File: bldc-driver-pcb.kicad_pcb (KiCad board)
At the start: 4 copper layers, 50 x 50 mm, 92 parts, among them IC1 ATSAMD21G18A-AFT, IC2 AS5047P-ATSM, IC3 L6498D, IC4 L6498D, IC5 L6498D, IC6 AD8030ARZ, IC7 AD8030ARZ, J1 FTSH-105-XX-X-DV, J2 505567-0471, J3 505567-0671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

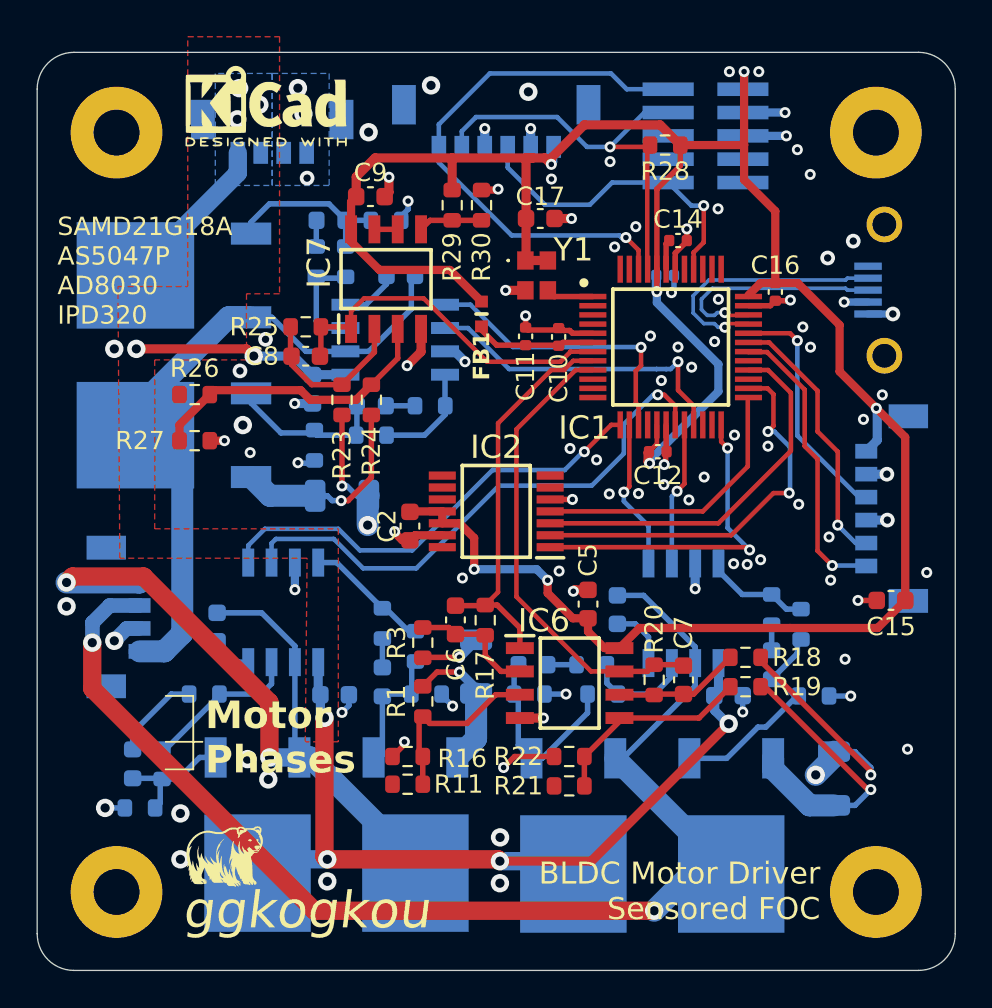
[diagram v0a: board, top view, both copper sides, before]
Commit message: Vmotor power plane
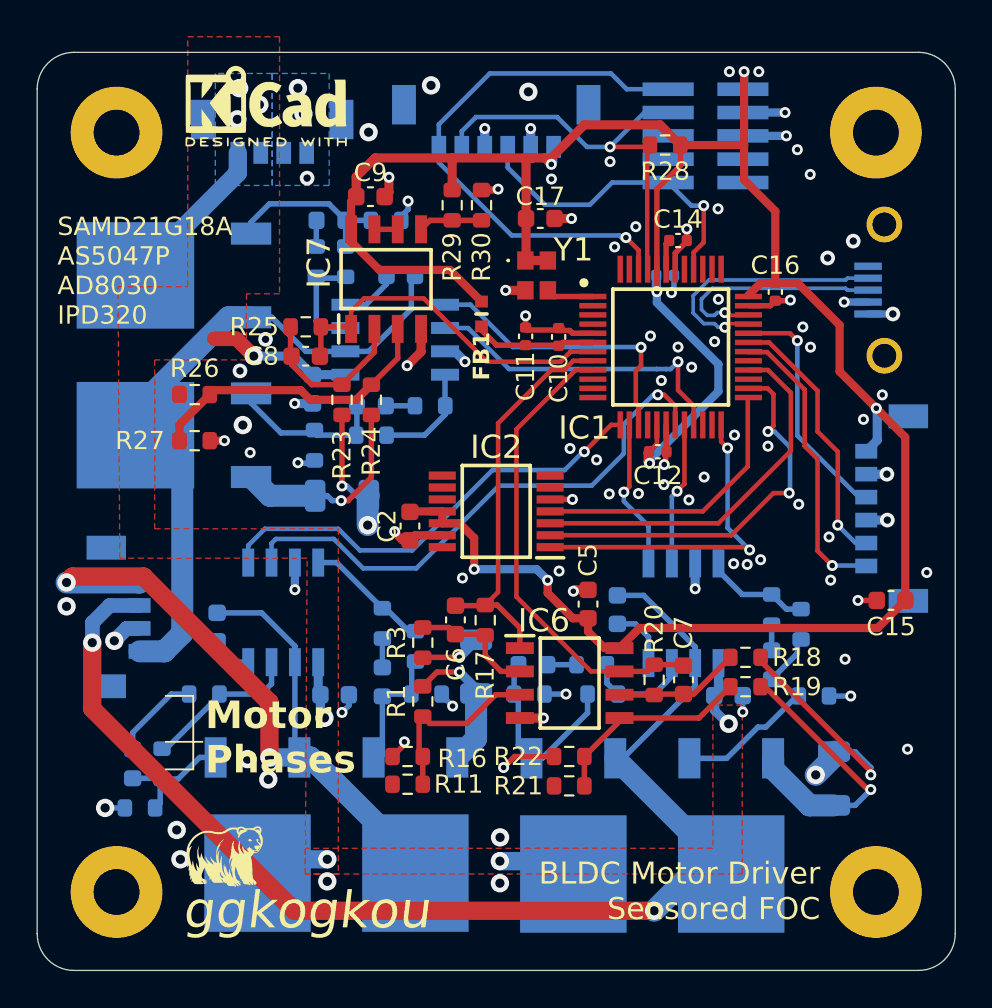
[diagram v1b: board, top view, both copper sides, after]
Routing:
- net VBUS: track 69.1 -> 32.3 mm, vias 9 -> 8
- net /Three-Phase Inverter/HALF_BRIDGE_2_OUT: track 69.6 -> 70.3 mm
- net GND: vias 104 -> 103
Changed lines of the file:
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@@
 		(tags "Connector")
 		(property "Reference" "J2"
-			(at 4 -3.2 0)
+			(at 5.8 1.8 0)
 			(layer "B.SilkS")
 			(effects
@@
 		(tags "resistor")
 		(property "Reference" "R14"
-			(at 1.05 1.2 270)
+			(at 0.05 1.25 270)
 			(layer "B.SilkS")
 			(effects
@@
 	)
 	(via
-		(at 122.8 116.9)
+		(at 122.6 117.8)
 		(size 1)
 		(drill 0.5)
@@
 	)
 	(via
-		(at 119.199997 91.6)
-		(size 1)
-		(drill 0.5)
-		(layers "F.Cu" "B.Cu")
-		(free yes)
-		(net 5)
-	)
-	(via
 		(at 149.9 91.499997)
 		(size 0.6)
@@
 	)
 	(segment
-		(start 145.177745 119.5)
-		(end 152.660638 112.017107)
-		(width 0.5)
-		(layer "F.Cu")
-		(net 11)
-	)
-	(segment
-		(start 130.644218 119.244218)
-		(end 130.8 119.4)
-		(width 1)
-		(layer "F.Cu")
-		(net 11)
-	)
-	(segment
-		(start 140.2 119.5)
-		(end 145.177745 119.5)
-		(width 0.5)
-		(layer "F.Cu")
-		(net 11)
-	)
-	(segment
 		(start 126.791806 91.99294)
-		(end 126.398866 91.6)
-		(width 0.5)
-		(layer "F.Cu")
-		(net 11)
-	)
-	(segment
-		(start 130.8 119.4)
-		(end 140.1 119.4)
-		(width 1)
-		(layer "F.Cu")
-		(net 11)
-	)
-	(segment
-		(start 126.398866 91.6)
-		(end 120.4 91.6)
-		(width 0.5)
-		(layer "F.Cu")
-		(net 11)
-	)
-	(segment
-		(start 140.1 119.4)
-		(end 140.2 119.5)
-		(width 1)
+		(end 125.848866 91.05)
+		(width 0.8)
 		(layer "F.Cu")
 		(net 11)
 	)
 	(segment
-		(start 130.644218 111.694087)
-		(end 130.644218 119.244218)
-		(width 1)
+		(start 125.848866 91.05)
+		(end 124.65 91.05)
+		(width 0.8)
 		(layer "F.Cu")
 		(net 11)
@@
 	)
 	(via
-		(at 120.4 91.6)
-		(size 1)
-		(drill 0.5)
-		(layers "F.Cu" "B.Cu")
-		(net 11)
-	)
-	(via
 		(at 140.2 119.5)
 		(size 1)
@@
 	)
 	(segment
-		(start 118 110.1)
-		(end 130.1 122.2)
+		(start 118 107.6)
+		(end 118 111.2)
 		(width 1)
 		(layer "F.Cu")
@@
 	)
 	(segment
-		(start 118 107.6)
-		(end 118 110.1)
+		(start 118 111.2)
+		(end 129 122.2)
 		(width 1)
 		(layer "F.Cu")
@@
 	)
 	(segment
-		(start 130.1 122.2)
+		(start 129 122.2)
 		(end 148.6 122.2)
 		(width 1)
@@
 			(pts
 				(xy 123.2 74.6) (xy 128.2 74.6) (xy 128.2 88.6) (xy 126.4 88.6) (xy 126.4 92.2) (xy 121.4 92.2)
-				(xy 121.4 101.4) (xy 131.4 101.4) (xy 131.4 113) (xy 129.6 113) (xy 129.7 103) (xy 119.5 103) (xy 119.4 88.2)
-				(xy 123.2 88.2)
+				(xy 121.4 101.4) (xy 131.4 101.4) (xy 131.4 120.2) (xy 129.6 120.2) (xy 129.7 103) (xy 119.5 103)
+				(xy 119.4 88.2) (xy 123.2 88.2)
+			)
+		)
+	)
+	(zone
+		(net 11)
+		(net_name "VBUS")
+		(layer "F.Cu")
+		(hatch edge 0.5)
+		(priority 5)
+		(connect_pads
+			(clearance 0.5)
+		)
+		(min_thickness 0.25)
+		(filled_areas_thickness no)
+		(fill yes
+			(thermal_gap 0.5)
+			(thermal_bridge_width 0.5)
+		)
+		(polygon
+			(pts
+				(xy 129.6 120.2) (xy 153.4 120.2) (xy 153.4 111) (xy 151.8 111) (xy 151.8 118.8) (xy 129.6 118.8)
 			)
 		)

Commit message: Layout QOL changes
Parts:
- moved R33 0.95 mm to (142.8, 110.4)
- moved C15 0.72 mm to (160.9, 105.8), turned to 0 degrees
- moved D3 0.70 mm to (142.7, 108.8)
- moved R7 0.62 mm to (145.8, 108.8)
- moved R1 0.43 mm to (136.0, 111.2)
- moved R11 0.41 mm to (135.2, 115.7)
- moved R31 0.37 mm to (121.0, 116.6)
- moved R16 0.34 mm to (135.2, 114.1)
- moved C5 0.23 mm to (145.1, 105.7), turned to 180 degrees
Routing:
- net /Three-Phase Inverter/HALF_BRIDGE_1_OUT: track 43.0 -> 37.5 mm
- net +3V3: track 141.2 -> 136.8 mm
- net GND: track 82.0 -> 83.7 mm, vias 103 -> 102
- net /Microcontroller/TCC0_WO2: track 16.0 -> 15.5 mm
- net Net-(D1-K): track 4.86 -> 4.32 mm
